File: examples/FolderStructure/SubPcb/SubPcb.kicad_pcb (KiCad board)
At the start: 2 copper layers, 8.8 x 0.8 mm, 3 parts, among them Q1 MMBT2222A

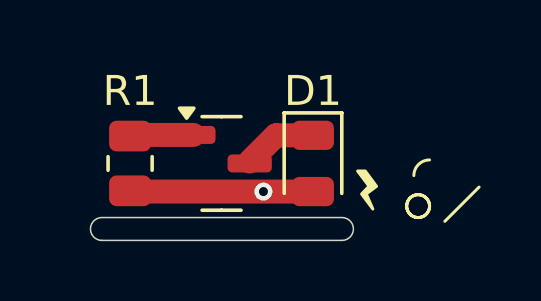
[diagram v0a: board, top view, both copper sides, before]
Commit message: Add Zones to Examples
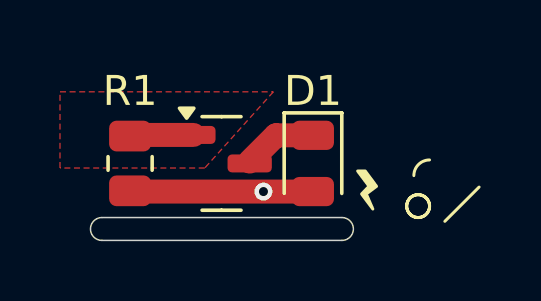
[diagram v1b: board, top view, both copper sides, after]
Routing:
- added copper zone on F.Cu, net /Input
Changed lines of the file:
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@@
 		(net 3)
 	)
+	(zone
+		(net 3)
+		(net_name "/Input")
+		(layer "F.Cu")
+		(hatch edge 0.5)
+		(priority 2)
+		(connect_pads
+			(clearance 0)
+		)
+		(min_thickness 0.25)
+		(filled_areas_thickness no)
+		(fill
+			(thermal_gap 0.5)
+			(thermal_bridge_width 0.5)
+		)
+		(polygon
+			(pts
+				(xy 17.526 15.494) (xy 24.638 15.494) (xy 22.352 18.034) (xy 17.526 18.034)
+			)
+		)
+	)
 )
